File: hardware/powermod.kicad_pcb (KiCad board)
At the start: 4 copper layers, 65 x 40 mm, 77 parts, among them J1 USB_C_IN, J2 USB_C_OUT, J3 JST_PH_2, J4 STEMMA_QT, J5 SWD_HDR, Q1 AON7407, Q2 AON7407, Q3 BSS138, SW1 BUTTON, U1 BM8563, U2 PY32F003F18P6, U3 TPS63020DSJR, U4 TP4056, U5 XC6206P332MR, Y1 32.768kHz

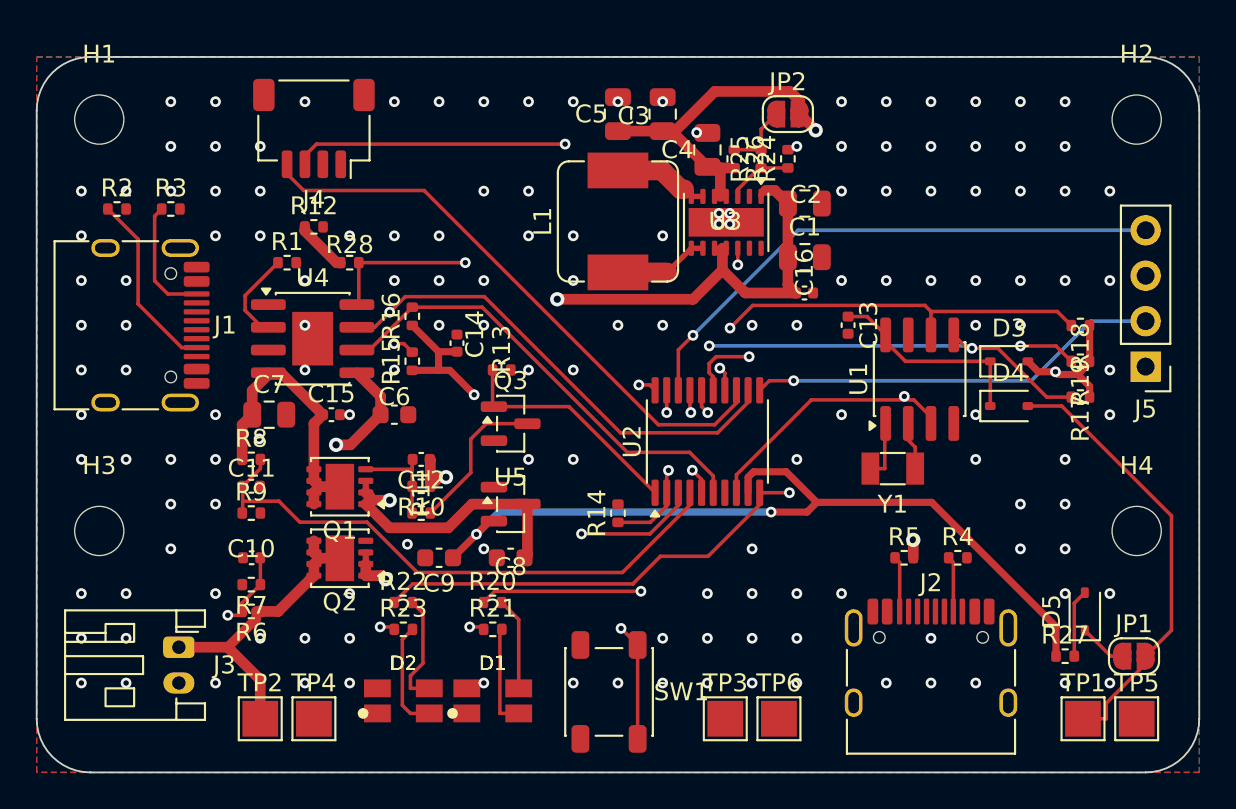
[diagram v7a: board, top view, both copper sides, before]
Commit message: hardware: recover user's finished board (escapes + L1N/L2 widened)
A reroute command's strip step ran+saved before the user interrupted it,
leaving the board stripped on disk. Restored from the pre-strip backup =
the user's finished board: USB-C VBUS/VOUT escapes routed, L1N/L2 re-widened
to uniform 1.1mm (track_width flags cleared), CC on the correct A8/B8 pads,
U3 EP tied (4 vias). 402 tracks, DRC 0 errors, pad-diff 226/226.

2 connections still open from the R2-R5 relocation: Q2.4 (VBUS gate) and
R4.2 (VOUT) - short local hops, to finish next.

Co-Authored-By: Claude Opus 4.8 <noreply@anthropic.com>
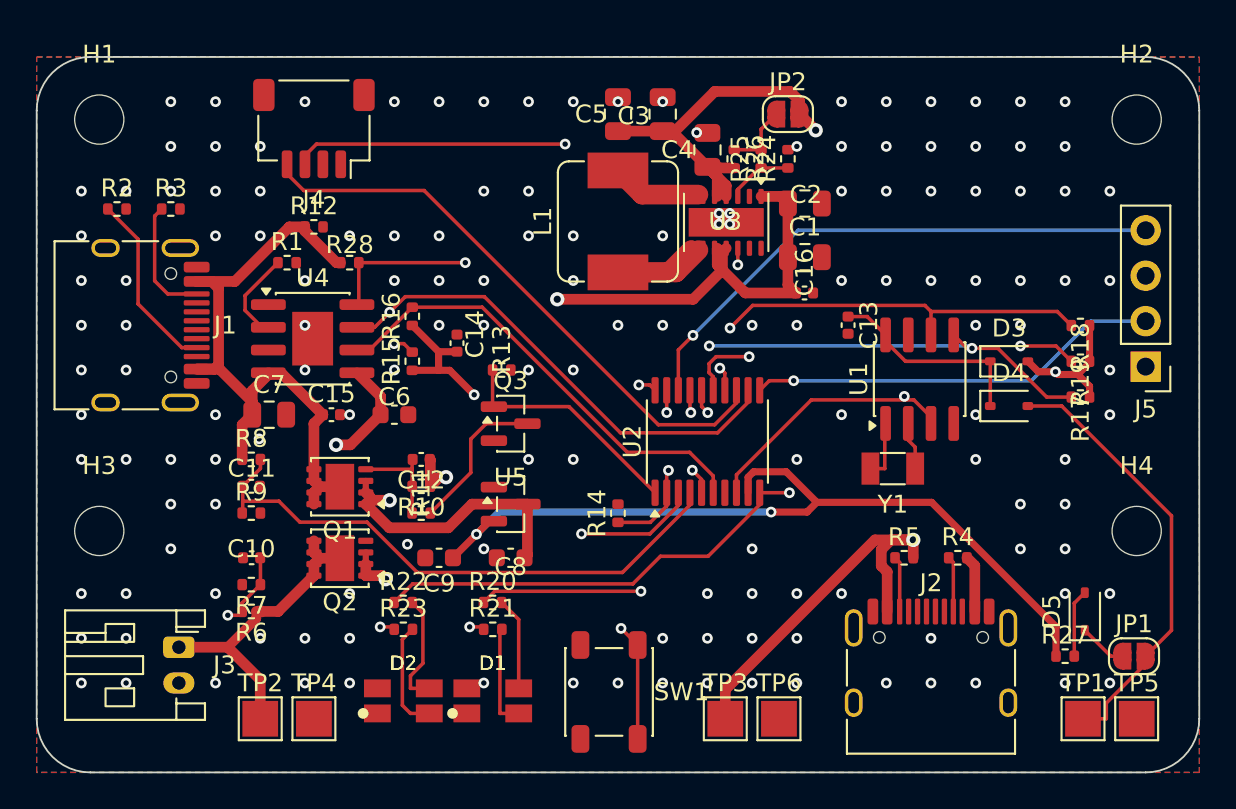
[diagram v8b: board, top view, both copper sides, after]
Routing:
- net VOUT: track 46.0 -> 72.1 mm
- net VBUS: track 19.0 -> 37.9 mm
- net L1N: track 5.31 -> 9.64 mm
- net VSYS: track 65.5 -> 66.0 mm
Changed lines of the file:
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@@
+	)
+	(segment
+		(start 9.95 17.45)
+		(end 8.945 17.45)
+		(width 0.6)
+		(layer "F.Cu")
+		(net "VBUS")
 	)
 	(segment
@@
 	)
 	(segment
+		(start 10.17 12.934748)
+		(end 10.17 17.23)
+		(width 0.6)
+		(layer "F.Cu")
+		(net "VBUS")
+	)
+	(segment
+		(start 8.945 12.55)
+		(end 9.785252 12.55)
+		(width 0.6)
+		(layer "F.Cu")
+		(net "VBUS")
+	)
+	(segment
+		(start 10.17 17.23)
+		(end 9.95 17.45)
+		(width 0.6)
+		(layer "F.Cu")
+		(net "VBUS")
+	)
+	(segment
+		(start 12.05 19.275)
+		(end 12.05 20)
+		(width 0.6)
+		(layer "F.Cu")
+		(net "VBUS")
+	)
+	(segment
 		(start 12.955 17.655)
 		(end 12.955 17.7522)
@@
 	)
 	(segment
+		(start 9.785252 12.55)
+		(end 10.17 12.934748)
+		(width 0.6)
+		(layer "F.Cu")
+		(net "VBUS")
+	)
+	(segment
 		(start 14.99 9.7233)
 		(end 14.99 9.5)
@@
 	)
 	(segment
+		(start 14.131371 9.5)
+		(end 14.99 9.5)
+		(width 0.6)
+		(layer "F.Cu")
+		(net "VBUS")
+	)
+	(segment
+		(start 11.081371 12.55)
+		(end 14.131371 9.5)
+		(width 0.6)
+		(layer "F.Cu")
+		(net "VBUS")
+	)
+	(segment
 		(start 15.5 25)
 		(end 15.5 24.35)
@@
 	)
 	(segment
+		(start 8.945 12.55)
+		(end 11.081371 12.55)
+		(width 0.6)
+		(layer "F.Cu")
+		(net "VBUS")
+	)
+	(segment
 		(start 12.955 17.7522)
 		(end 12.05 18.6572)
@@
 	)
 	(segment
+		(start 10.225 17.45)
+		(end 12.05 19.275)
+		(width 0.6)
+		(layer "F.Cu")
+		(net "VBUS")
+	)
+	(segment
 		(start 15.5 24.35)
 		(end 15.825 24.025)
+		(width 0.6)
+		(layer "F.Cu")
+		(net "VBUS")
+	)
+	(segment
+		(start 8.945 17.45)
+		(end 10.225 17.45)
 		(width 0.6)
 		(layer "F.Cu")
@@
 	)
 	(segment
-		(start 38.4 10.695)
-		(end 38.3998 10.695)
-		(width 0.6)
-		(layer "F.Cu")
-		(net "VSYS")
-	)
-	(segment
 		(start 22.5142 23.4958)
 		(end 22.01 24)
@@
 	)
 	(segment
-		(start 38.3402 10.695)
-		(end 38.3998 10.695)
-		(width 0.3004)
-		(layer "F.Cu")
-		(net "VSYS")
-	)
-	(segment
 		(start 27.275 28)
 		(end 27.4375 27.8375)
-		(width 0.6)
-		(layer "F.Cu")
-		(net "VSYS")
-	)
-	(segment
-		(start 41.2652 7.4602)
-		(end 42 8.195)
 		(width 0.6)
 		(layer "F.Cu")
@@
 	)
 	(segment
+		(start 41.6 7.795)
+		(end 40.5 7.795)
+		(width 0.6)
+		(layer "F.Cu")
+		(net "VSYS")
+	)
+	(segment
 		(start 18.4 24.35)
 		(end 18.4 23.7)
@@
 	)
 	(segment
-		(start 38.4 10.695)
-		(end 38.55 10.695)
-		(width 0.3004)
-		(layer "F.Cu")
-		(net "VSYS")
-	)
-	(segment
 		(start 27.4375 27.8375)
 		(end 27.4375 25)
@@
 	)
 	(segment
-		(start 40.75 7.4602)
-		(end 40.5 7.7102)
-		(width 0.3004)
-		(layer "F.Cu")
-		(net "VSYS")
-	)
-	(segment
-		(start 40.75 7.4602)
-		(end 41.2652 7.4602)
+		(start 38.3402 11.9107)
+		(end 38.0498 11.6203)
 		(width 0.6)
 		(layer "F.Cu")
@@
 	)
 	(segment
+		(start 38.3402 10.9048)
+		(end 38.55 10.695)
+		(width 0.6)
+		(layer "F.Cu")
+		(net "VSYS")
+	)
+	(segment
 		(start 19.7356 24.7832)
 		(end 18.6168 24.7832)
@@
 	)
 	(segment
-		(start 37.9 10.695)
-		(end 38.3402 10.695)
-		(width 0.3004)
-		(layer "F.Cu")
-		(net "VSYS")
-	)
-	(segment
 		(start 18.4 24.35)
 		(end 18.6168 24.5668)
@@
 	)
 	(segment
+		(start 42 8.195)
+		(end 41.6 7.795)
+		(width 0.6)
+		(layer "F.Cu")
+		(net "VSYS")
+	)
+	(segment
 		(start 24.3388 25)
 		(end 23.0159 26.3229)
@@
 		(start 18.4 29)
 		(end 18.4 28.35)
+		(width 0.6)
+		(layer "F.Cu")
+		(net "VSYS")
+	)
+	(segment
+		(start 38.0498 11.6203)
+		(end 38.0498 10.695)
+		(width 0.6)
+		(layer "F.Cu")
+		(net "VSYS")
+	)
+	(segment
+		(start 38.3402 11.9107)
+		(end 38.3402 10.9048)
 		(width 0.6)
 		(layer "F.Cu")
@@
 	)
 	(segment
-		(start 38.3402 10.695)
-		(end 38.3402 11.9107)
-		(width 0.6)
-		(layer "F.Cu")
-		(net "VSYS")
-	)
-	(segment
 		(start 18.6168 24.5668)
 		(end 18.6168 24.7832)
@@
 	)
 	(segment
+		(start 38.0498 6.6948)
+		(end 38.0498 7.795)
+		(width 0.6)
+		(layer "F.Cu")
+		(net "VOUT")
+	)
+	(segment
 		(start 37.56 6.205)
 		(end 37.5 6.145)
@@
 	)
 	(segment
+		(start 52.45 28.44)
+		(end 52.01 28)
+		(width 0.6)
+		(layer "F.Cu")
+		(net "VOUT")
+	)
+	(segment
 		(start 35.0349 4.1799)
 		(end 35 4.145)
@@
 	)
 	(segment
+		(start 38.5 37)
+		(end 38.5 35.368629)
+		(width 0.6)
+		(layer "F.Cu")
+		(net "VOUT")
+	)
+	(segment
 		(start 42.1183 1.9279)
 		(end 42.65 2.4596)
@@
 	)
 	(segment
+		(start 47.55 31.005)
+		(end 47.55 28.781768)
+		(width 0.6)
+		(layer "F.Cu")
+		(net "VOUT")
+	)
+	(segment
+		(start 47.767332 27.0009)
+		(end 49.01 27.0009)
+		(width 0.6)
+		(layer "F.Cu")
+		(net "VOUT")
+	)
+	(segment
 		(start 35.6566 4.3016)
 		(end 35.6566 4.1799)
@@
 	)
 	(segment
-		(start 38.225 7.795)
-		(end 38.225 6.205)
+		(start 37.5 6.145)
+		(end 38.55 7.195)
 		(width 0.6)
 		(layer "F.Cu")
@@
 	)
 	(segment
-		(start 38.55 7.795)
-		(end 38.225 7.795)
-		(width 0.3004)
-		(layer "F.Cu")
-		(net "VOUT")
-	)
-	(segment
-		(start 38.225 7.795)
-		(end 37.9 7.795)
-		(width 0.3004)
+		(start 38.55 7.195)
+		(end 38.55 7.795)
+		(width 0.6)
+		(layer "F.Cu")
+		(net "VOUT")
+	)
+	(segment
+		(start 52.45 31.005)
+		(end 52.45 28.44)
+		(width 0.6)
+		(layer "F.Cu")
+		(net "VOUT")
+	)
+	(segment
+		(start 47.22 28.451768)
+		(end 47.22 27.548232)
+		(width 0.6)
 		(layer "F.Cu")
 		(net "VOUT")
@@
 	)
 	(segment
+		(start 46.867729 27.0009)
+		(end 49.01 27.0009)
+		(width 0.6)
+		(layer "F.Cu")
+		(net "VOUT")
+	)
+	(segment
+		(start 37.5 6.145)
+		(end 38.0498 6.6948)
+		(width 0.6)
+		(layer "F.Cu")
+		(net "VOUT")
+	)
+	(segment
 		(start 35.6566 4.1799)
 		(end 35.0349 4.1799)
@@
 	)
 	(segment
+		(start 38.5 35.368629)
+		(end 46.867729 27.0009)
+		(width 0.6)
+		(layer "F.Cu")
+		(net "VOUT")
+	)
+	(segment
+		(start 47.55 28.781768)
+		(end 47.22 28.451768)
+		(width 0.6)
+		(layer "F.Cu")
+		(net "VOUT")
+	)
+	(segment
 		(start 39 6.205)
 		(end 38.225 6.205)
+		(width 0.6)
+		(layer "F.Cu")
+		(net "VOUT")
+	)
+	(segment
+		(start 47.22 27.548232)
+		(end 47.767332 27.0009)
 		(width 0.6)
 		(layer "F.Cu")
@@
 	)
 	(segment
-		(start 36.0029 7.3962)
-		(end 36.2012 7.3962)
+		(start 33.85 7.695)
+		(end 36.9998 7.695)
 		(width 1.1)
 		(layer "F.Cu")
@@
 	)
 	(segment
-		(start 36.2012 7.3962)
-		(end 36.6 7.795)
-		(width 0.3004)
+		(start 32.5 6.345)
+		(end 33.85 7.695)
+		(width 1.1)
 		(layer "F.Cu")
 		(net "L2")
 	)
 	(segment
-		(start 34.9517 6.345)
-		(end 36.0029 7.3962)
+		(start 35.35 12.045)
+		(end 36.6 10.795)
 		(width 1.1)
 		(layer "F.Cu")
-		(net "L2")
-	)
-	(segment
-		(start 37.25 7.795)
-		(end 36.6 7.795)
-		(width 0.3004)
-		(layer "F.Cu")
-		(net "L2")
-	)
-	(segment
-		(start 32.5 6.345)
-		(end 34.9517 6.345)
+		(net "L1N")
+	)
+	(segment
+		(start 32.5 12.045)
+		(end 35.7498 12.045)
 		(width 1.1)
 		(layer "F.Cu")
-		(net "L2")
-	)
-	(segment
-		(start 36.6 10.695)
-		(end 37.25 10.695)
-		(width 0.3004)
-		(layer "F.Cu")
 		(net "L1N")
 	)
 	(segment
 		(start 32.5 12.045)
-		(end 35.25 12.045)
+		(end 35.35 12.045)
 		(width 1.1)
 		(layer "F.Cu")
@@
 	)
 	(segment
-		(start 35.25 12.045)
-		(end 36.6 10.695)
-		(width 0.3004)
+		(start 35.7498 12.045)
+		(end 36.9998 10.795)
+		(width 1.1)
 		(layer "F.Cu")
 		(net "L1N")
